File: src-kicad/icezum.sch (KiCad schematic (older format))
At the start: 1 part

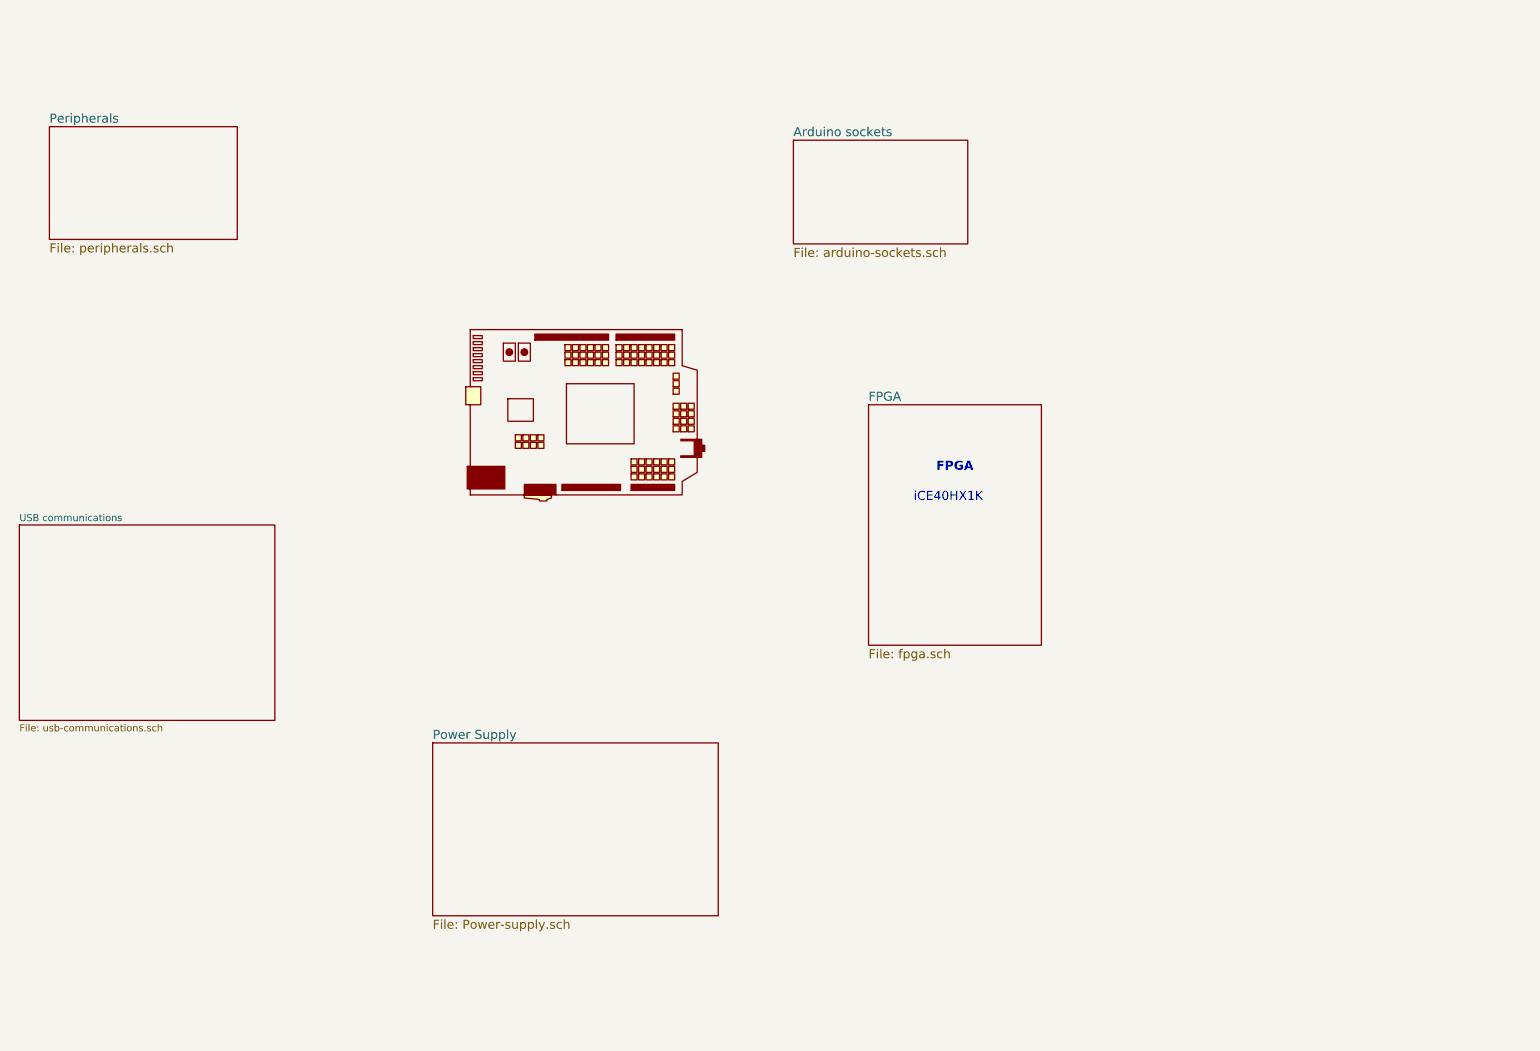
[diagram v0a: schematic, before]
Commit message: Kicad schematic: top sheet refactored
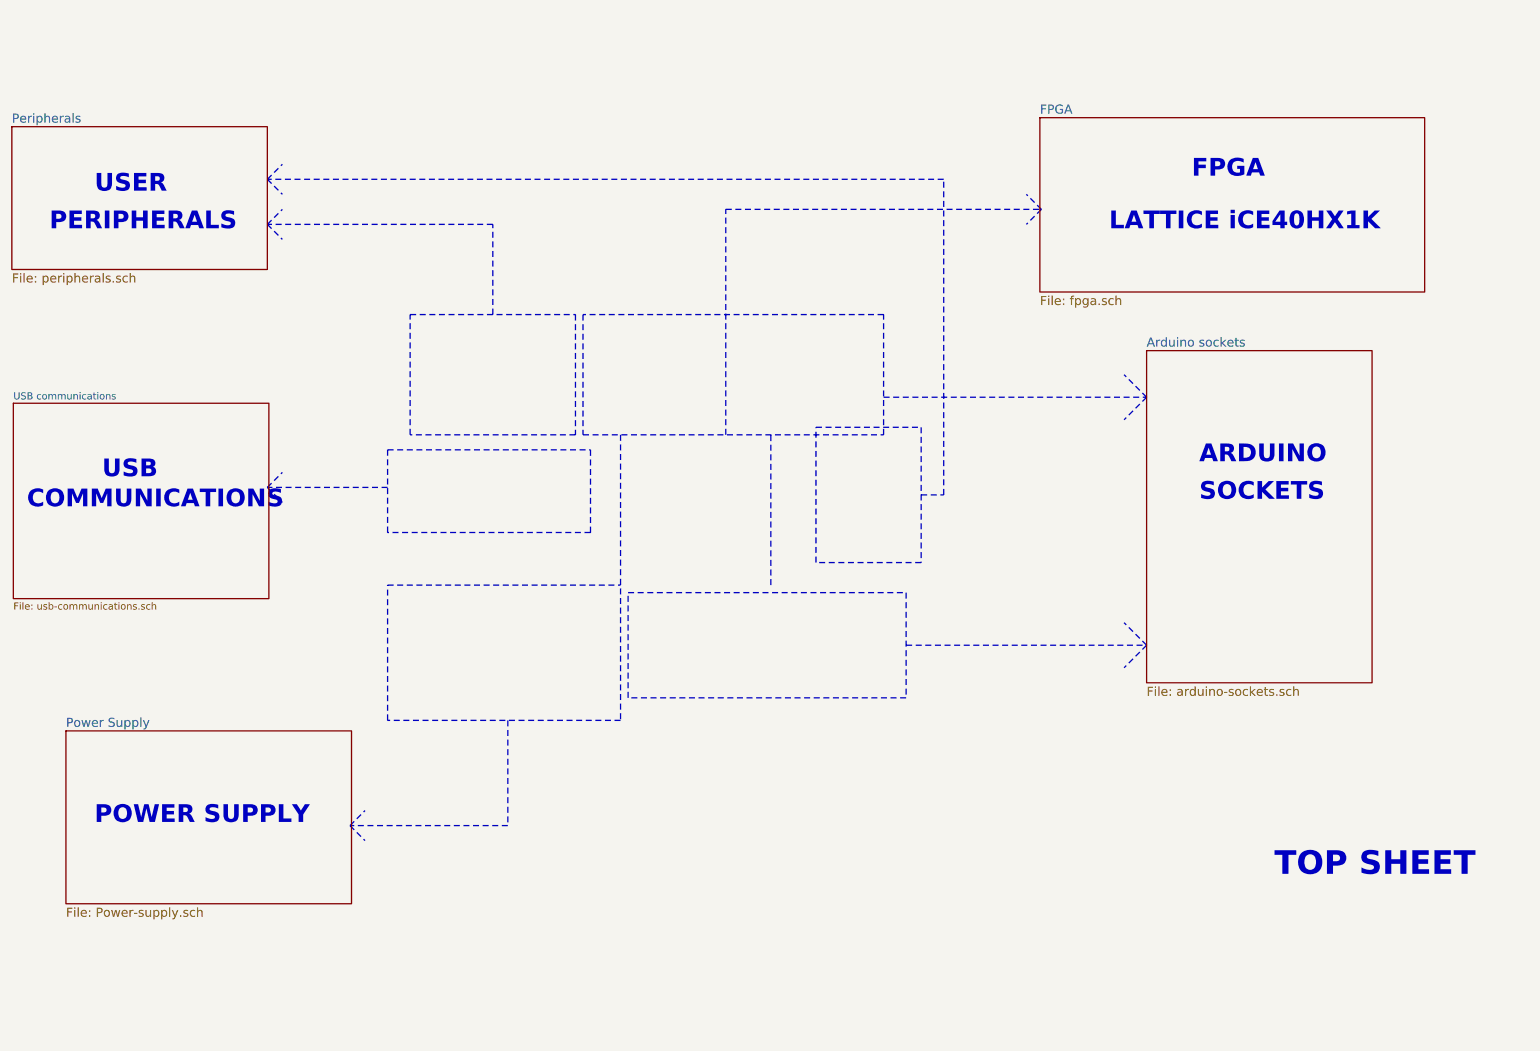
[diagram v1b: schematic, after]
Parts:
- removed DOC2: icezum-headers-doc, symbol icezum-headers-doc
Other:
- note added: "ARDUINO"
- note added: "COMMUNICATIONS"
- note added: "LATTICE iCE40HX1K"
- note added: "PERIPHERALS"
- note added: "POWER SUPPLY"
- note added: "SOCKETS"
- note added: "TOP SHEET"
- note added: "USB"
- note added: "USER"
- note removed: "iCE40HX1K"

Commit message: Kicad schematic: fpga sheet: aligned to 50mils grid
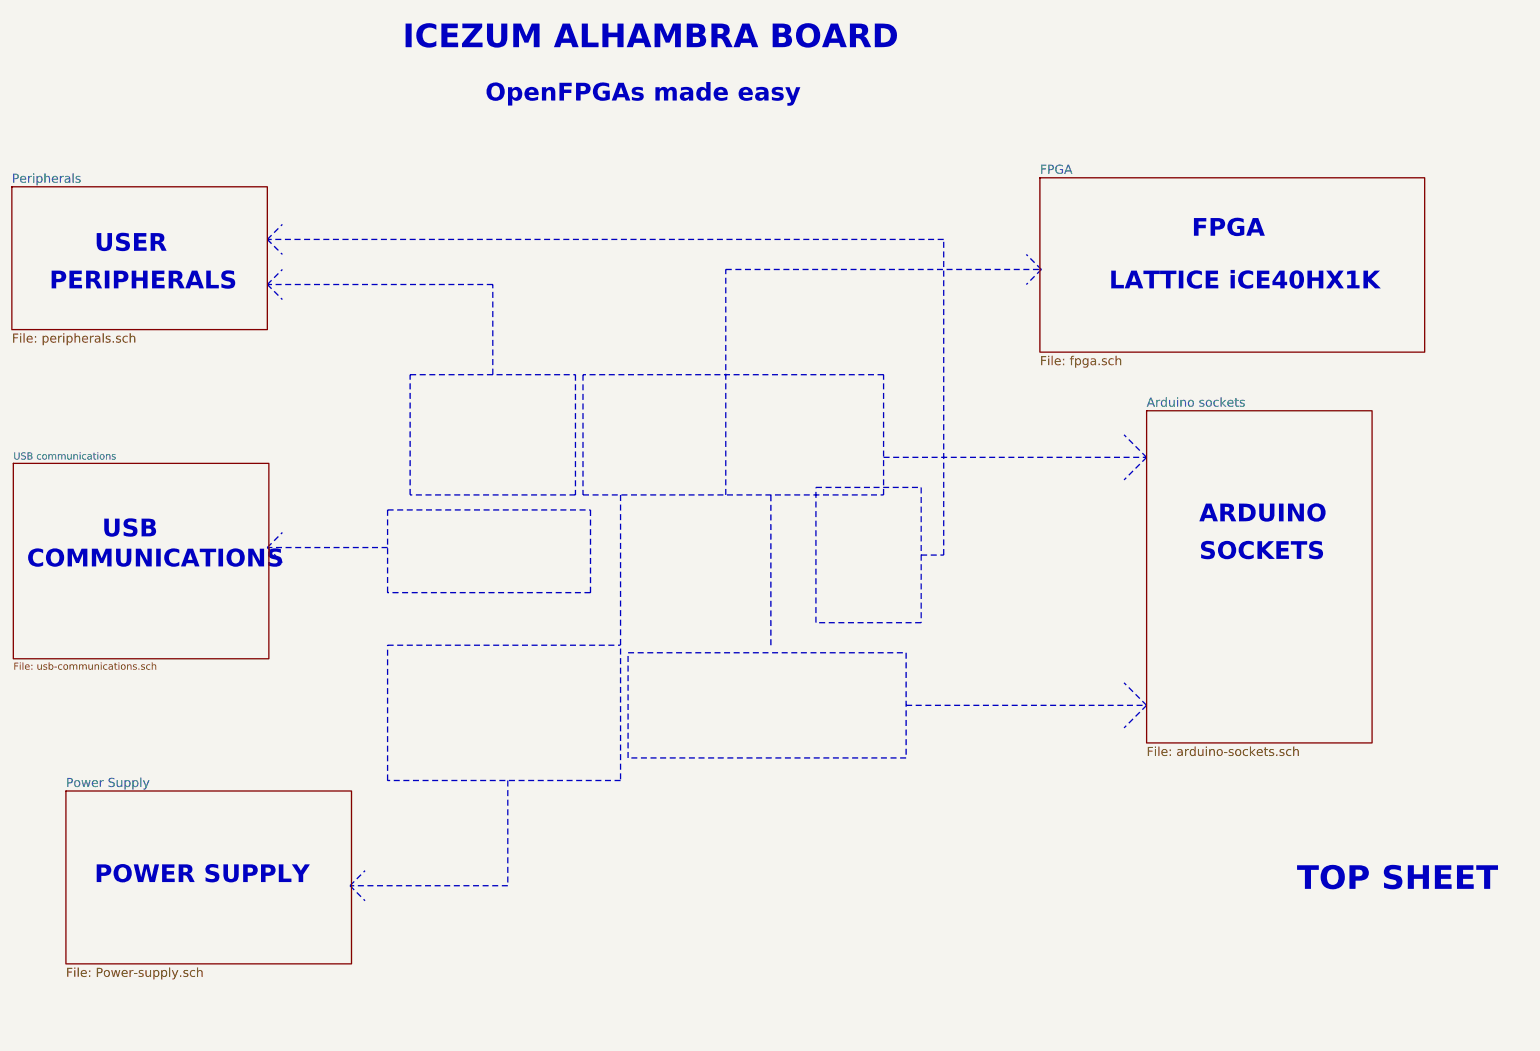
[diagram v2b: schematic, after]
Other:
- note added: "ICEZUM ALHAMBRA BOARD"
- note added: "OpenFPGAs made easy"
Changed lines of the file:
@@
 Title "IceZUM Alhambra FPGA board (TOP SHEET)"
 Date "2016-05-23"
-Rev "1.0-kicad"
+Rev "1.0-kicad-1"
 Comp "FPGAwars"
 Comment1 "Migration to kicad:  Juan Gonzalez (Obijuan)"
@@
 $EndDescr
 $Sheet
-S 8140 1290 2560 1160
+S 8140 1690 2560 1160
 U 5742A672
 F0 "FPGA" 60
@@
 $EndSheet
 $Sheet
-S 8850 2840 1500 2210
+S 8850 3240 1500 2210
 U 57455C58
 F0 "Arduino sockets" 60
@@
 $EndSheet
 $Sheet
-S 1660 5370 1900 1150
+S 1660 5770 1900 1150
 U 574540C9
 F0 "Power Supply" 60
@@
 $EndSheet
 $Sheet
-S 1300 1350 1700 950
+S 1300 1750 1700 950
 U 57489FE9
 F0 "Peripherals" 60
@@
 $EndSheet
 $Sheet
-S 1310 3190 1700 1300
+S 1310 3590 1700 1300
 U 574C0DEC
 F0 "USB communications" 47
@@
 EndData
 $EndBitmap
-Text Notes 9700 6350 0    157  ~ 31
+Text Notes 9850 6450 0    157  ~ 31
 TOP SHEET
 $Bitmap
-Pos 5600 3900
+Pos 5600 4300
 Scale 1,000000
 Data
@@
 00 00 00 40 72 80 D8 1D 00 00 00 00 00 80 E4 00 B1 3B 00 00 00 00 00 00 C9 01 62 77 00 00 00 00
 00 00 92 03 C4 EE 00 00 00 00 00 00 24 87 FF 07 15 01 18 D9 BC B4 8D 10 00 00 00 00 49 45 4E 44
-AE 42 60 82 00
+AE 42 60 82 25
 EndData
 $EndBitmap
 Wire Notes Line
-	3800 4400 5350 4400
+	3800 4800 5350 4800
 Wire Notes Line
-	5350 3400 5350 5300
+	5350 3800 5350 5700
 Wire Notes Line
-	5350 5300 3800 5300
+	5350 5700 3800 5700
 Wire Notes Line
-	3800 5300 3800 4400
+	3800 5700 3800 4800
 Wire Notes Line
-	4600 5300 4600 6000
+	4600 5700 4600 6400
 Wire Notes Line
-	4600 6000 3550 6000
+	4600 6400 3550 6400
 Wire Notes Line
-	3550 6000 3650 5900
+	3550 6400 3650 6300
 Wire Notes Line
-	3550 6000 3650 6100
-Text Notes 1850 6000 0    118  ~ 24
+	3550 6400 3650 6500
+Text Notes 1850 6400 0    118  ~ 24
 POWER SUPPLY
 Wire Notes Line
-	3800 3500 5150 3500
+	3800 3900 5150 3900
 Wire Notes Line
-	5150 3500 5150 4050
+	5150 3900 5150 4450
 Wire Notes Line
-	5150 4050 3800 4050
+	5150 4450 3800 4450
 Wire Notes Line
-	3800 4050 3800 3500
+	3800 4450 3800 3900
 Wire Notes Line
-	3800 3750 3000 3750
+	3800 4150 3000 4150
 Wire Notes Line
-	3000 3750 3100 3650
+	3000 4150 3100 4050
 Wire Notes Line
-	3000 3750 3100 3850
-Text Notes 1900 3700 0    118  ~ 24
+	3000 4150 3100 4250
+Text Notes 1900 4100 0    118  ~ 24
 USB
-Text Notes 1400 3900 0    118  ~ 24
+Text Notes 1400 4300 0    118  ~ 24
 COMMUNICATIONS
 Wire Notes Line
-	6650 3350 7350 3350
+	6650 3750 7350 3750
 Wire Notes Line
-	7350 3350 7350 4250
+	7350 3750 7350 4650
 Wire Notes Line
-	7350 4250 6650 4250
+	7350 4650 6650 4650
 Wire Notes Line
-	6650 4250 6650 3350
+	6650 4650 6650 3750
 Wire Notes Line
-	3950 2600 5050 2600
+	3950 3000 5050 3000
 Wire Notes Line
-	5050 2600 5050 3400
+	5050 3000 5050 3800
 Wire Notes Line
-	5050 3400 3950 3400
+	5050 3800 3950 3800
 Wire Notes Line
-	3950 3400 3950 2600
-Text Notes 1850 1800 0    118  ~ 24
+	3950 3800 3950 3000
+Text Notes 1850 2200 0    118  ~ 24
 USER
-Text Notes 1550 2050 0    118  ~ 24
+Text Notes 1550 2450 0    118  ~ 24
 PERIPHERALS
 Wire Notes Line
-	4500 2600 4500 2000
+	4500 3000 4500 2400
 Wire Notes Line
-	4500 2000 3000 2000
+	4500 2400 3000 2400
 Wire Notes Line
-	7350 3800 7500 3800
+	7350 4200 7500 4200
 Wire Notes Line
-	7500 3800 7500 1700
+	7500 4200 7500 2100
 Wire Notes Line
-	7500 1700 3000 1700
-Text Notes 9200 3600 0    118  ~ 24
+	7500 2100 3000 2100
+Text Notes 9200 4000 0    118  ~ 24
 ARDUINO
-Text Notes 9200 3850 0    118  ~ 24
+Text Notes 9200 4250 0    118  ~ 24
 SOCKETS
 Wire Notes Line
-	5100 2600 5100 3400
+	5100 3000 5100 3800
 Wire Notes Line
-	5100 3400 7100 3400
+	5100 3800 7100 3800
 Wire Notes Line
-	7100 3400 7100 2600
+	7100 3800 7100 3000
 Wire Notes Line
-	7100 2600 5100 2600
+	7100 3000 5100 3000
 Wire Notes Line
-	5400 4450 7250 4450
+	5400 4850 7250 4850
 Wire Notes Line
-	7250 4450 7250 5150
+	7250 4850 7250 5550
 Wire Notes Line
-	7250 5150 5400 5150
+	7250 5550 5400 5550
 Wire Notes Line
-	5400 5150 5400 4450
+	5400 5550 5400 4850
 Wire Notes Line
-	7250 4800 8850 4800
+	7250 5200 8850 5200
 Wire Notes Line
-	7100 3150 8850 3150
+	7100 3550 8850 3550
 Wire Notes Line
-	6350 4400 6350 3400
+	6350 4800 6350 3800
 Wire Notes Line
-	6050 3400 6050 1900
+	6050 3800 6050 2300
 Wire Notes Line
-	6050 1900 8150 1900
-Text Notes 8600 2050 0    118  ~ 24
+	6050 2300 8150 2300
+Text Notes 8600 2450 0    118  ~ 24
 LATTICE iCE40HX1K
-Text Notes 9150 1700 0    118  ~ 24
+Text Notes 9150 2100 0    118  ~ 24
 FPGA
 Wire Notes Line
-	8850 3150 8700 3000
+	8850 3550 8700 3400
 Wire Notes Line
-	8850 3150 8700 3300
+	8850 3550 8700 3700
 Wire Notes Line
-	8850 4800 8700 4650
+	8850 5200 8700 5050
 Wire Notes Line
-	8850 4800 8700 4950
+	8850 5200 8700 5350
 Wire Notes Line
-	8150 1900 8050 1800
+	8150 2300 8050 2200
 Wire Notes Line
-	8150 1900 8050 2000
+	8150 2300 8050 2400
 Wire Notes Line
-	3000 1700 3100 1600
+	3000 2100 3100 2000
 Wire Notes Line
-	3000 1700 3100 1800
+	3000 2100 3100 2200
 Wire Notes Line
-	3000 2000 3100 1900
+	3000 2400 3100 2300
 Wire Notes Line
-	3000 2000 3100 2100
+	3000 2400 3100 2500
+Text Notes 3900 850  0    157  ~ 31
+ICEZUM ALHAMBRA BOARD
+Text Notes 4450 1200 0    118  ~ 24
+OpenFPGAs made easy
 $EndSCHEMATC

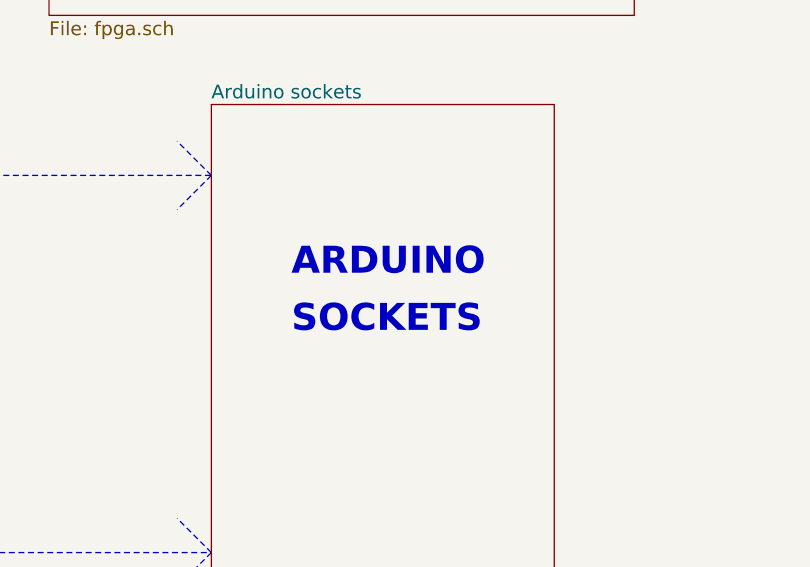
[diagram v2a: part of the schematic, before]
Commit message: Kicad schematic: added fpgawars logo and CC-BY-SA to all the sheets
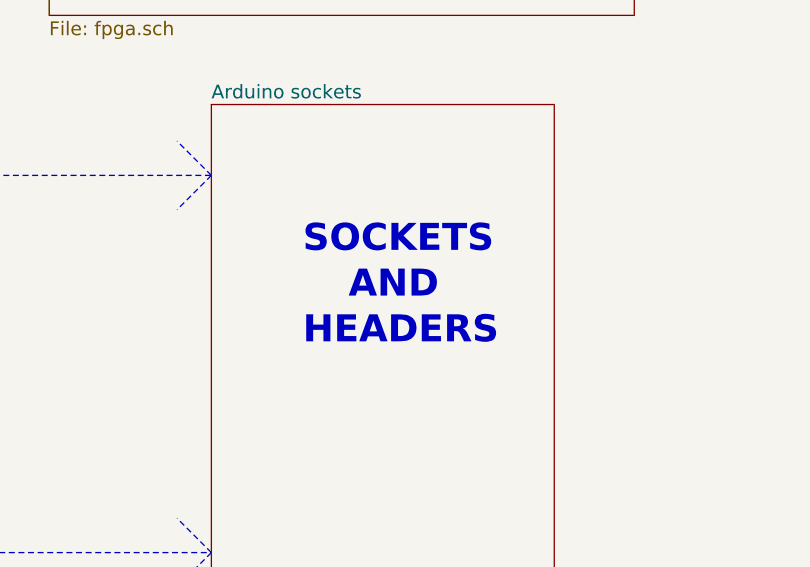
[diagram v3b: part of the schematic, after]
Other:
- note added: "AND\n"
- note added: "HEADERS\n"
- note removed: "ARDUINO"
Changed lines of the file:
@@
 Wire Notes Line
 	7500 2100 3000 2100
-Text Notes 9200 4000 0    118  ~ 24
-ARDUINO
-Text Notes 9200 4250 0    118  ~ 24
+Text Notes 9250 3900 0    118  ~ 24
 SOCKETS
 Wire Notes Line
@@
 Text Notes 4450 1200 0    118  ~ 24
 OpenFPGAs made easy
+Text Notes 9450 4100 0    118  ~ 24
+AND\n
+Text Notes 9250 4300 0    118  ~ 24
+HEADERS\n
 $EndSCHEMATC

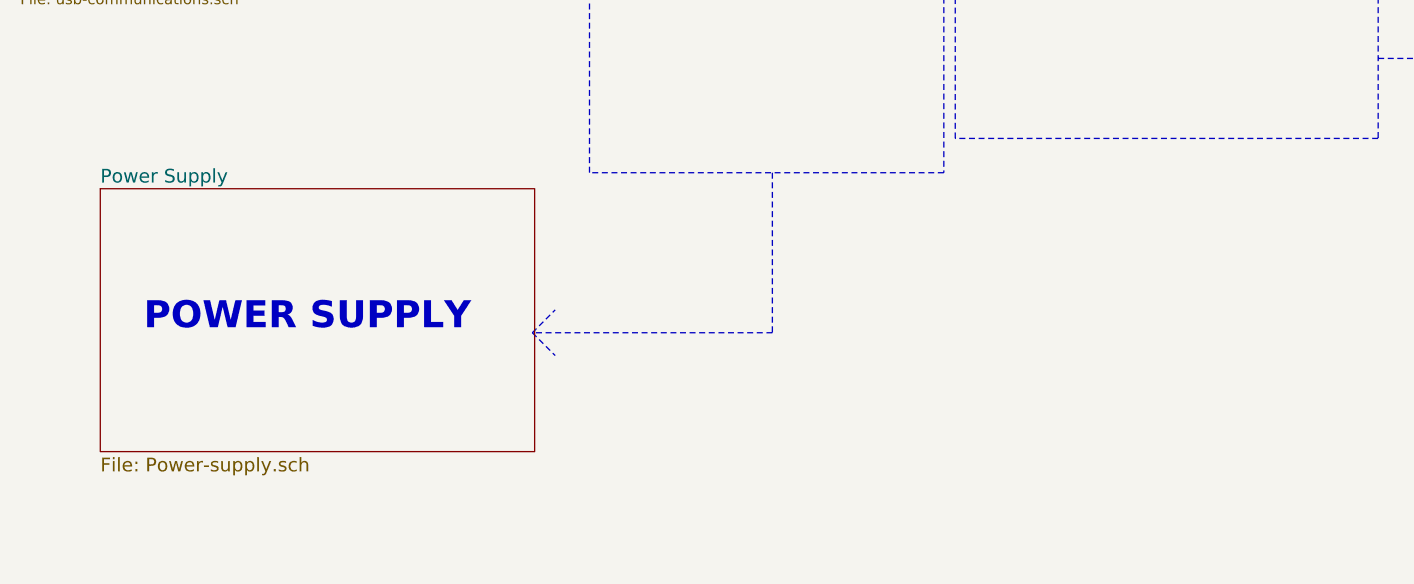
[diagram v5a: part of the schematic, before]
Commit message: Kicad schematic: block diagram added
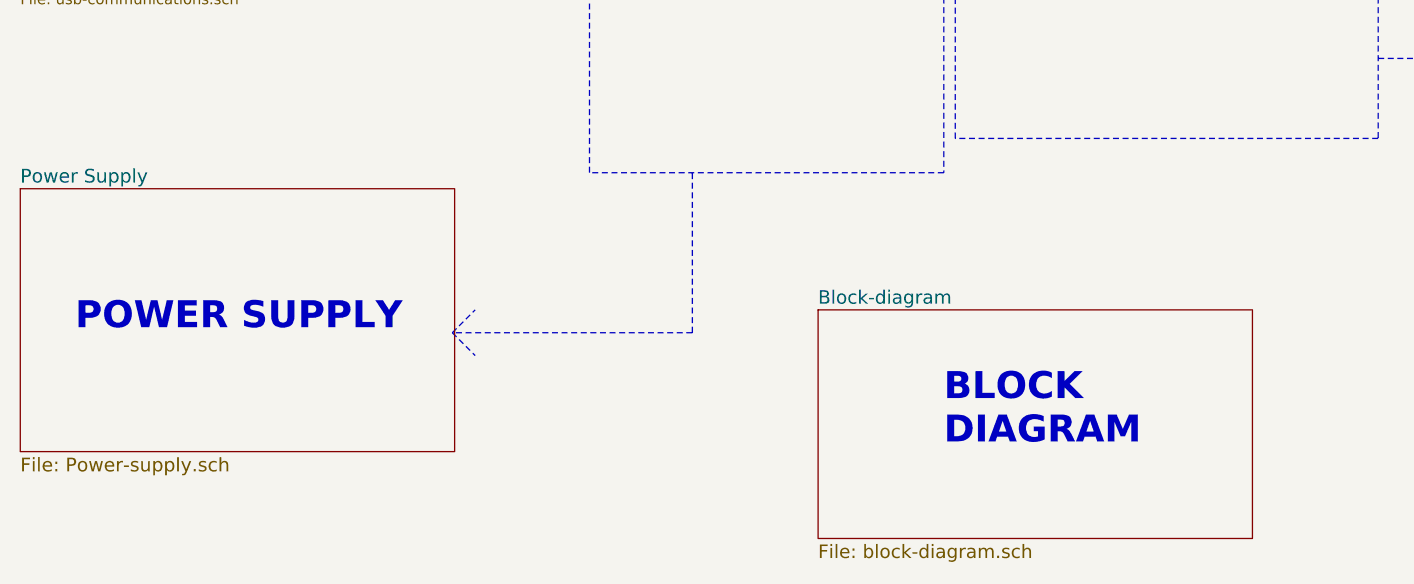
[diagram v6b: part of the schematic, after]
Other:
- note added: "BLOCK\nDIAGRAM"
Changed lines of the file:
@@
 EESchema Schematic File Version 2
 LIBS:icezum
-LIBS:icezum-cache
 EELAYER 25 0
 EELAYER END
 $Descr A4 11693 8268
 encoding utf-8
-Sheet 1 6
+Sheet 1 7
 Title "IceZUM Alhambra FPGA board (TOP SHEET)"
 Date "2016-05-23"
@@
 $EndSheet
 $Sheet
-S 1660 5770 1900 1150
+S 1310 5770 1900 1150
 U 574540C9
 F0 "Power Supply" 60
@@
 F3 F0 1D 79 17 0B BC D0 AE 96 03 B8 3F 0C 6D B8 A2 A8 0B 16 2C 58 B0 60 C1 82 05 0B 16 2C 58 B0
 60 C1 82 05 0B 16 2C 58 B0 E0 7F 81 FF 00 64 C5 01 8A 14 5C 86 66 00 00 00 00 49 45 4E 44 AE 42
-60 82 FD
+60 82 46
 EndData
 $EndBitmap
@@
 00 00 00 40 72 80 D8 1D 00 00 00 00 00 80 E4 00 B1 3B 00 00 00 00 00 00 C9 01 62 77 00 00 00 00
 00 00 92 03 C4 EE 00 00 00 00 00 00 24 87 FF 07 15 01 18 D9 BC B4 8D 10 00 00 00 00 49 45 4E 44
-AE 42 60 82 00
+AE 42 60 82 FF
 EndData
 $EndBitmap
@@
 	3800 5700 3800 4800
 Wire Notes Line
-	4600 5700 4600 6400
+	4250 6400 3200 6400
 Wire Notes Line
-	4600 6400 3550 6400
+	3200 6400 3300 6300
 Wire Notes Line
-	3550 6400 3650 6300
-Wire Notes Line
-	3550 6400 3650 6500
-Text Notes 1850 6400 0    118  ~ 24
+	3200 6400 3300 6500
+Text Notes 1550 6400 0    118  ~ 24
 POWER SUPPLY
 Wire Notes Line
@@
 Text Notes 9250 4300 0    118  ~ 24
 HEADERS\n
+$Sheet
+S 4800 6300 1900 1000
+U 574C12D9
+F0 "Block-diagram" 59
+F1 "block-diagram.sch" 59
+$EndSheet
+Text Notes 5350 6900 0    118  ~ 24
+BLOCK\nDIAGRAM
+Wire Notes Line
+	4250 6400 4250 5700
 $EndSCHEMATC
